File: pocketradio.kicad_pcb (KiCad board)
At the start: 2 copper layers, 30 x 30 mm, 23 parts, among them CN1 PJ-320D, U1 SI4702-C19-GMR, U2 CH32V003F4U6, U3 TPA6130A2RTJR

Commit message: lots of stuff
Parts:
- added BT1: MY-2032-12, easyeda2kicad:BAT-SMD_MY-2032-12, B.Cu at (142.6, 62.2)
- added J1: Conn_01x03_Pin, Connector_PinHeader_2.54mm:PinHeader_1x03_P2.54mm_Vertical, F.Cu at (129.8, 58.8)
- added R1: 10k, Resistor_SMD:R_0603_1608Metric, F.Cu at (149.8, 69.2)
- added R2: 10k, Resistor_SMD:R_0603_1608Metric, F.Cu at (154.4, 69.2)
- added R3: 10k, Resistor_SMD:R_0603_1608Metric, F.Cu at (145.0, 69.2)
- added R4: 10k, Resistor_SMD:R_0603_1608Metric, F.Cu at (140.4, 69.2)
- added SW1: SW_Push_45deg, easyeda2kicad:SW-SMD_4P-L4.2-W3.3-P2.15-LS5.1, F.Cu at (149.7, 73.0)
- added SW2: SW_Push_45deg, easyeda2kicad:SW-SMD_4P-L4.2-W3.3-P2.15-LS5.1, F.Cu at (154.4, 73.0)
- added SW3: SW_Push_45deg, easyeda2kicad:SW-SMD_4P-L4.2-W3.3-P2.15-LS5.1, F.Cu at (145.0, 73.0)
- added SW4: SW_Push_45deg, easyeda2kicad:SW-SMD_4P-L4.2-W3.3-P2.15-LS5.1, F.Cu at (140.4, 73.0)
- added SW5: K3-2235S-F1, easyeda2kicad:SW-SMD_MST22D18G2, F.Cu at (132.7, 72.7)
- moved C7 24.2 mm to (139.0, 49.4), turned to 90 degrees
- moved C8 21.1 mm to (136.6, 50.2)
- moved U2 18.8 mm to (137.2, 53.8), turned to 90 degrees
- moved C5 17.2 mm to (133.6, 52.4), turned to -90 degrees
- moved U3 16.3 mm to (148.6, 61.8), turned to -90 degrees
- moved R8 13.7 mm to (144.7, 59.6), turned to 180 degrees
- moved C1 13.0 mm to (134.2, 65.9), turned to 180 degrees
- moved R9 12.8 mm to (144.7, 60.6)
- moved FB1 12.7 mm to (141.6, 51.0), turned to -90 degrees
- moved R10 12.1 mm to (144.7, 61.6)
- moved R6 11.3 mm to (139.5, 63.0)
- moved L1 11.3 mm to (147.0, 57.8), turned to -90 degrees
- moved C2 10.8 mm to (149.1, 58.6)
- moved FB2 9.33 mm to (142.4, 56.8), turned to 180 degrees
- moved C6 9.05 mm to (154.2, 61.8), turned to 180 degrees
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- renumbered C4 to C2, C5 to C3, C6 to C4, C7 to C5, C3 to C6, C9 to C7, C2 to C9, R8 to R10, R1 to R5, R2 to R6, R3 to R7, R4 to R8, R7 to R9, U2 to U1, U3 to U2, U1 to U3
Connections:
- U1 pad 17: unconnected-(U2-PD3-Pad17) -> /PD3
- U1 pad 18: unconnected-(U2-PD4-Pad18) -> /PD4
- U1 pad 19: unconnected-(U2-PD5-Pad19) -> /PD5
- U1 pad 20: unconnected-(U2-PD6-Pad20) -> /PD6
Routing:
- net +3V3: track 0.00 -> 108.0 mm, vias 0 -> 7
- net Net-(BT1-Pad1): track 0.00 -> 63.2 mm, vias 0 -> 1
- net /PD3: track 0.00 -> 43.0 mm, vias 0 -> 2
- net /PD4: track 0.00 -> 36.0 mm, vias 0 -> 2
- net /PD5: track 0.00 -> 29.4 mm, vias 0 -> 2
- net /RF_RST: track 0.00 -> 27.7 mm, vias 0 -> 2
- net GND: track 0.00 -> 27.6 mm, vias 0 -> 5
- net /SEN: track 0.00 -> 24.1 mm, vias 0 -> 2
- net /PD6: track 0.00 -> 22.6 mm
- net /L_RAW: track 0.00 -> 21.9 mm
- net /SDA: track 0.00 -> 21.9 mm, vias 0 -> 2
- net /SCL: track 0.00 -> 21.4 mm, vias 0 -> 2
- net /R_RAW: track 0.00 -> 17.4 mm
- net /SWDEBUG: track 0.00 -> 9.39 mm
- net /RCLK: track 0.00 -> 5.48 mm, vias 0 -> 2
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- added copper zone on F.Cu, net GND
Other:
- outline, holes or cut-outs redrawn
- board text added: "Designed by Alex Park"
- board text added: "Sussy Radio Keychain Rev 1"

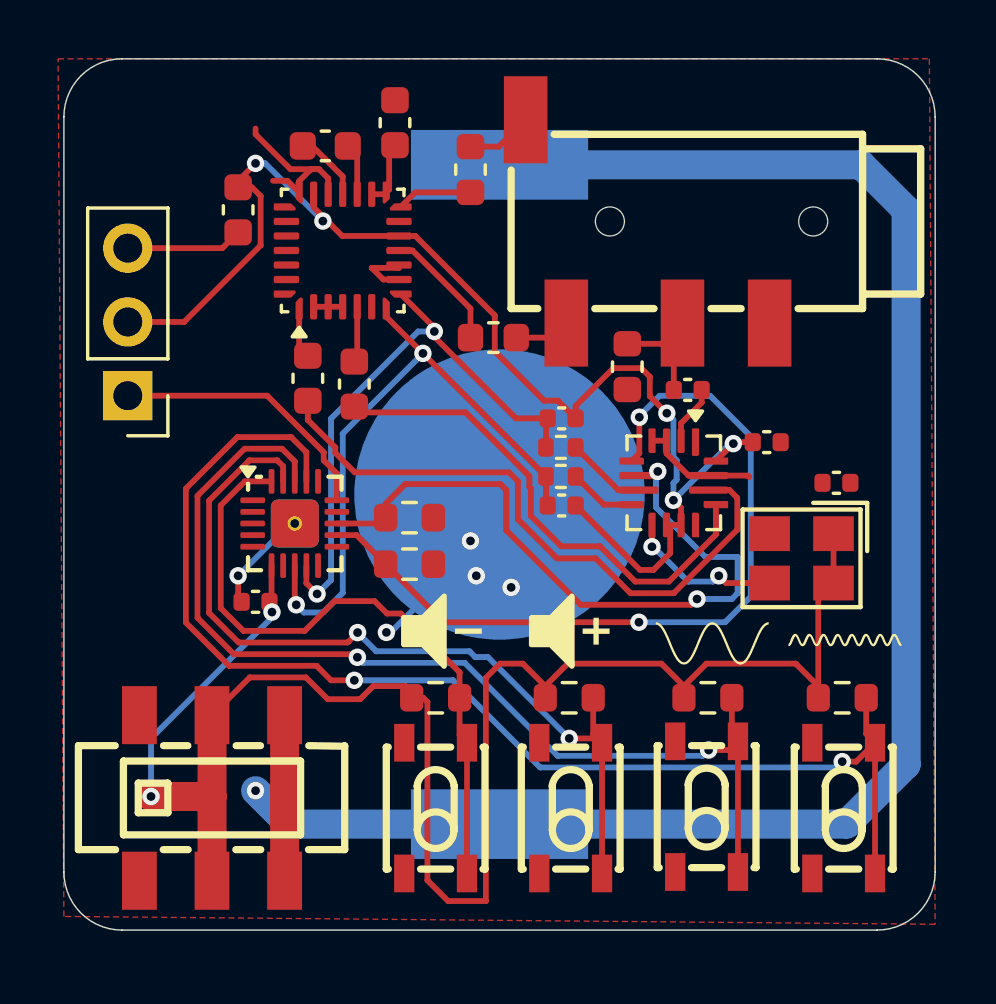
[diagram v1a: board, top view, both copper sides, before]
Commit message: power LED
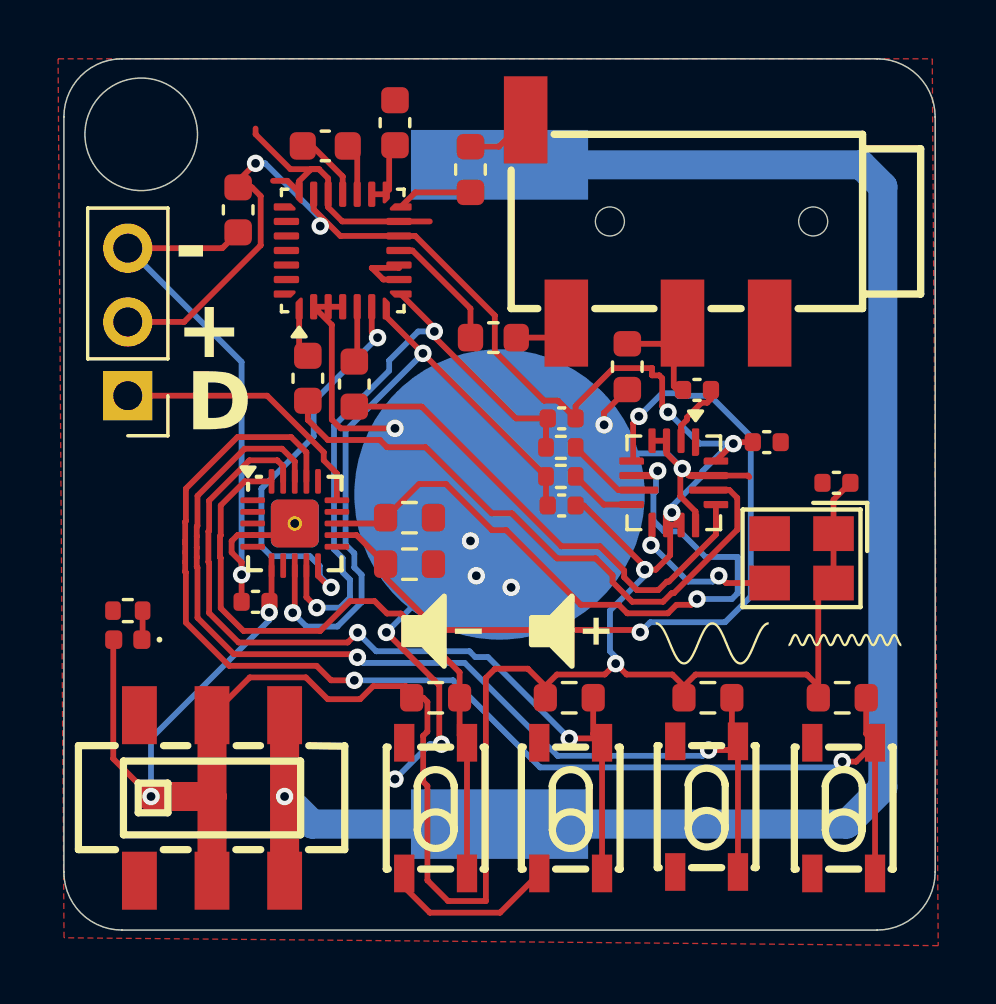
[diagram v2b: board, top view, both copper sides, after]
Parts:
- added D1: LED, LED_SMD:LED_0402_1005Metric, F.Cu at (129.8, 67.2)
- added R11: 330, Resistor_SMD:R_0402_1005Metric, F.Cu at (129.8, 66.2)
- moved C2 0.32 mm to (149.4, 58.6)
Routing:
- net GND: track 27.6 -> 80.6 mm, vias 5 -> 10
- net /SD: track 0.00 -> 14.1 mm, vias 0 -> 2
- net +3V3: track 108.0 -> 119.6 mm, vias 7 -> 9
- net /SCL: track 21.4 -> 23.3 mm
- net Net-(BT1-Pad1): track 63.2 -> 61.4 mm
- net /SDA: track 21.9 -> 23.6 mm
- net Net-(D1-K): track 0.00 -> 1.01 mm
- net /RF_RST: track 27.7 -> 28.4 mm
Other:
- outline, holes or cut-outs redrawn
- board text added: "+"
- board text added: "-"
- board text added: "D"
- board text added: "Design by Alex Park"
- board text removed: "Designed by Alex Park"

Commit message: recheck audio jack pinou
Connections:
- CN1 pad 2: unconnected-(CN1-Pad2) -> Net-(C2-Pad1)
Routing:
- net Net-(C2-Pad1): track 4.87 -> 7.87 mm
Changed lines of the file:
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@@
 			(size 3 1.5)
 			(layers "F.Cu" "F.Mask" "F.Paste")
-			(net "unconnected-(CN1-Pad2)")
+			(net "Net-(C2-Pad1)")
 			(pinfunction "2_2")
-			(pintype "unspecified+no_connect")
+			(pintype "unspecified")
 		)
 		(pad "3" smd rect
@@
 		)
 		(embedded_fonts no)
-		(model "${KIPRJMOD}/JLCImport.3dshapes/PJ-320D.wrl"
+		(model "${KIPRJMOD}/JLCImport.3dshapes/PJ-320D.step"
 			(offset
-				(xyz -3.200013 0 2.55)
+				(xyz -7.900013 0 3.05)
 			)
 			(scale
@@
 			)
 			(rotate
-				(xyz 0 0 0)
+				(xyz -0 -0 -0)
 			)
 		)
@@
 		)
 		(embedded_fonts no)
-		(model "${KICAD10_3DMODEL_DIR}/Package_DFN_QFN.3dshapes/QFN-28_4x4mm_P0.5mm.step"
+		(model "${KICAD10_3DMODEL_DIR}/Package_DFN_QFN.3dshapes/QFN-24_4x4mm_P0.5mm.step"
 			(offset
 				(xyz 0 0 0)
@@
 			)
 			(rotate
-				(xyz 0 0 0)
+				(xyz -0 -0 -0)
 			)
 		)
@@
 		(width 0.2)
 		(layer "F.Cu")
+		(net "Net-(C2-Pad1)")
+	)
+	(segment
+		(start 148.900127 56.300127)
+		(end 151.900127 56.300127)
+		(width 0.2)
+		(layer "F.Cu")
